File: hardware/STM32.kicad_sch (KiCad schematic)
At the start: 15 parts, among them U1 STM32U595RJTxQ

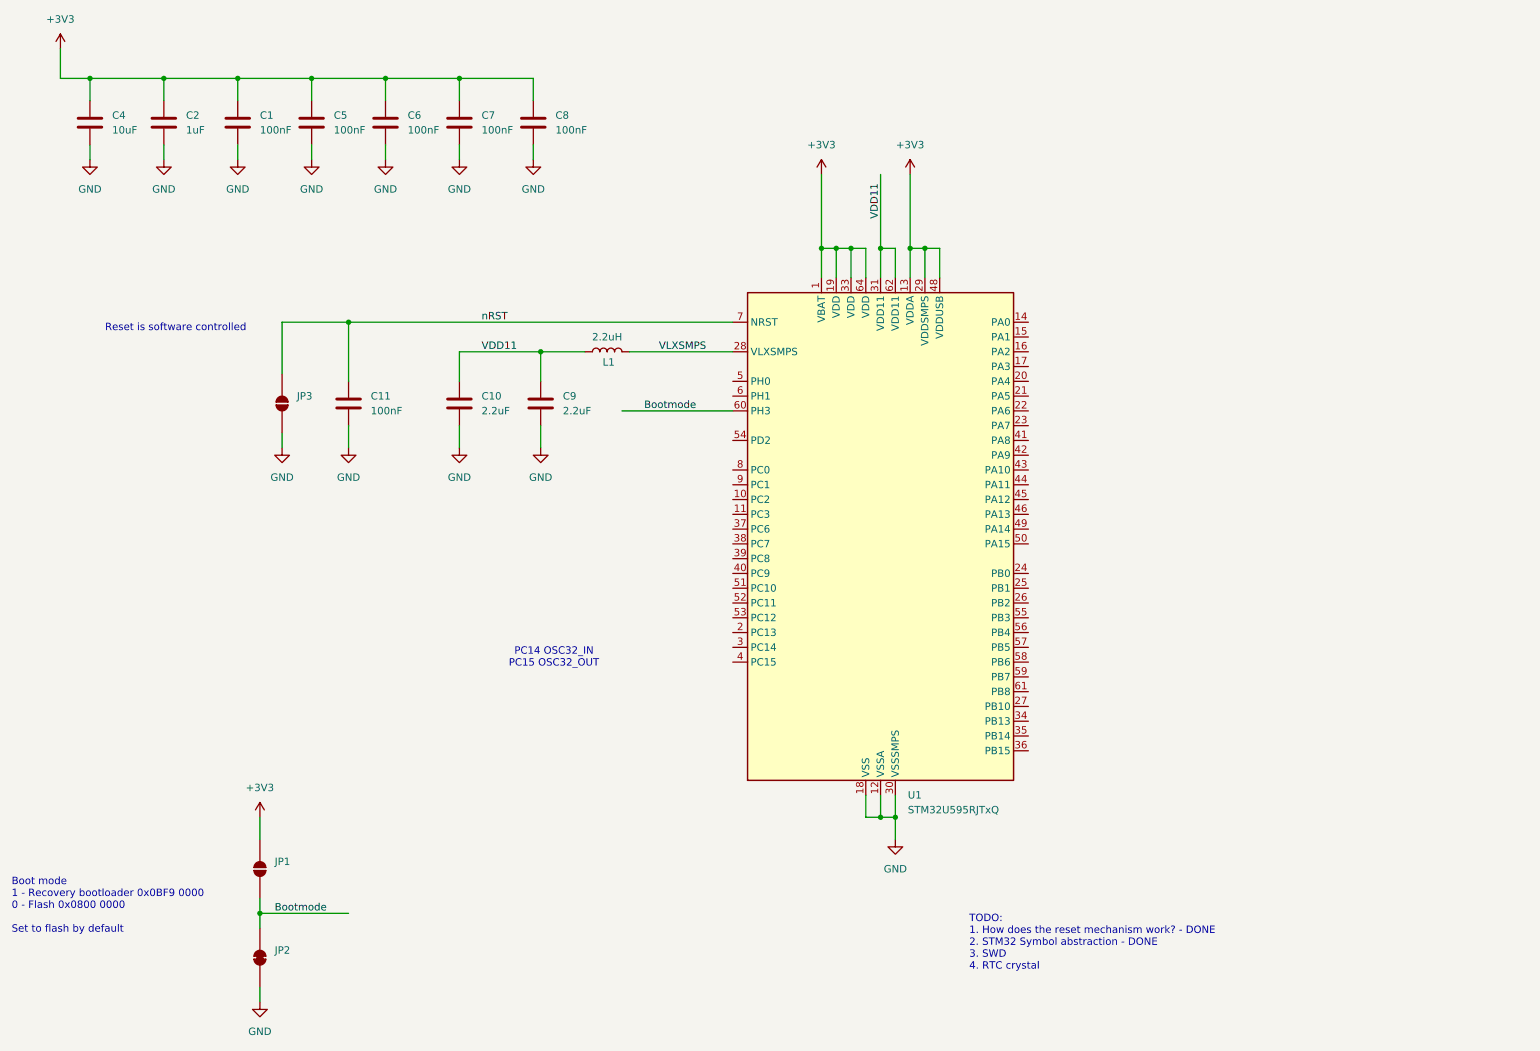
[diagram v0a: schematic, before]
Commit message: Completed STM32 schematic
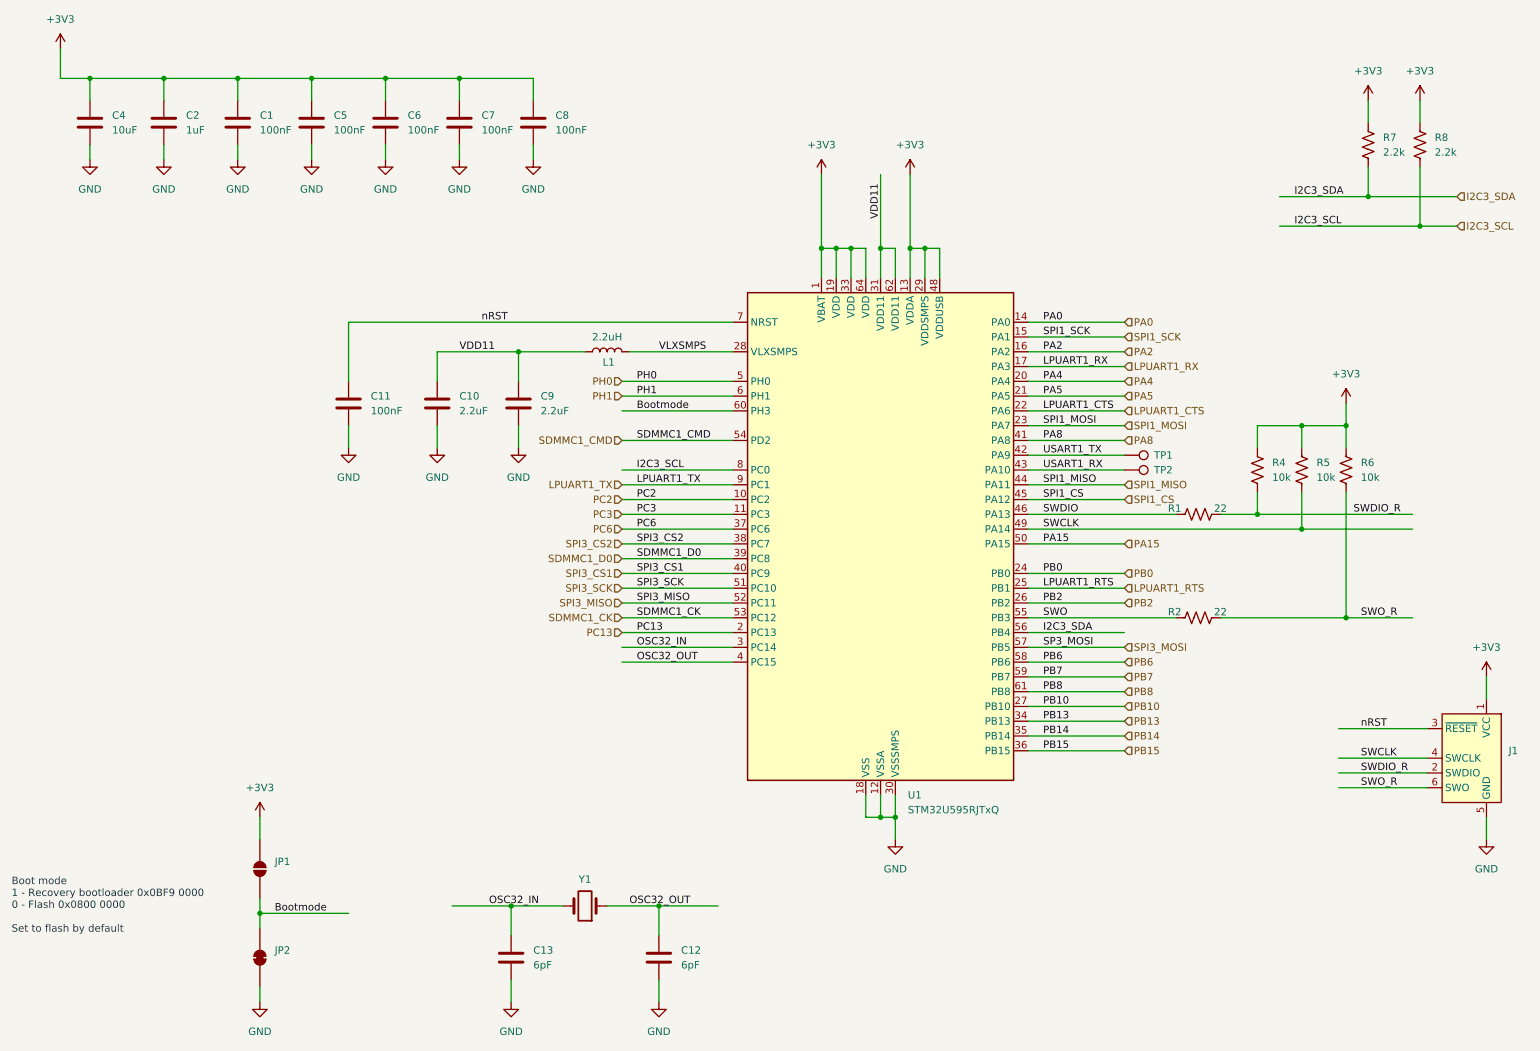
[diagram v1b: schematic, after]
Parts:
- removed JP3: SolderJumper_2_Open, symbol Jumper:SolderJumper_2_Open
- added C12, C13: 6pF, symbol Device:C
- added J1: Conn_ARM_SWD_TagConnect_TC2030-NL, Connector:Tag-Connect_TC2030-IDC-NL_2x03_P1.27mm_Vertical, symbol Connector:Conn_ARM_SWD_TagConnect_TC2030-NL
- added R1, R2: 22, symbol Device:R_US
- added R4, R5, R6: 10k, symbol Device:R_US
- added R7, R8: 2.2k, symbol Device:R_US
- added TP1, TP2: TestPoint, symbol Connector:TestPoint
- added Y1: ECS-.327-6-12R-TR, symbol Device:Crystal
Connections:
- net +3V3: now also J1.1 (VCC), R4.2, R5.2, R6.2, R7.2, R8.2
- net GND: now also C12.2, C13.2, J1.5 (GND)
- net nRST: now also J1.3 (~{RESET})
- net PC2: now reaches U1.10 (PC2)
- net PC3: now reaches U1.11 (PC3)
- net PA0: now reaches U1.14 (PA0)
- net SPI1_SCK: now reaches U1.15 (PA1)
- net PA2: now reaches U1.16 (PA2)
- net LPUART1_RX: now reaches U1.17 (PA3)
- net PC13: now reaches U1.2 (PC13)
- net PA4: now reaches U1.20 (PA4)
- net PA5: now reaches U1.21 (PA5)
- net LPUART1_CTS: now reaches U1.22 (PA6)
- net SPI1_MOSI: now reaches U1.23 (PA7)
- net PB0: now reaches U1.24 (PB0)
- net LPUART1_RTS: now reaches U1.25 (PB1)
- net PB2: now reaches U1.26 (PB2)
- net PB10: now reaches U1.27 (PB10)
- net OSC32_IN: now reaches U1.3 (PC14)
- net OSC32_IN: now also C13.1, Y1.2
- net PB13: now reaches U1.34 (PB13)
- net PB14: now reaches U1.35 (PB14)
- net PB15: now reaches U1.36 (PB15)
- net PC6: now reaches U1.37 (PC6)
- net SPI3_CS2: now reaches U1.38 (PC7)
- net SDMMC1_D0: now reaches U1.39 (PC8)
- net OSC32_OUT: now reaches U1.4 (PC15)
- net OSC32_OUT: now also C12.1, Y1.1
- net SPI3_CS1: now reaches U1.40 (PC9)
- net PA8: now reaches U1.41 (PA8)
- net USART1_TX: now reaches U1.42 (PA9)
- net USART1_TX: now also TP1.1
- net USART1_RX: now reaches U1.43 (PA10)
- net USART1_RX: now also TP2.1
- net SPI1_MISO: now reaches U1.44 (PA11)
- net SPI1_CS: now reaches U1.45 (PA12)
- net SWDIO: now reaches U1.46 (PA13)
- net SWDIO: now also R1.1
- net SWCLK: now reaches U1.49 (PA14)
- net SWCLK: now also J1.4 (SWCLK), R5.1
- net PH0: now reaches U1.5 (PH0)
- net PA15: now reaches U1.50 (PA15)
- net SPI3_SCK: now reaches U1.51 (PC10)
- net SPI3_MISO: now reaches U1.52 (PC11)
- net SDMMC1_CK: now reaches U1.53 (PC12)
- net SDMMC1_CMD: now reaches U1.54 (PD2)
- net SWO: now reaches U1.55 (PB3)
- net SWO: now also R2.1
- net I2C3_SDA: now reaches U1.56 (PB4)
- net I2C3_SDA: now also R7.1
- net SPI3_MOSI: now reaches U1.57 (PB5)
- net PB6: now reaches U1.58 (PB6)
- net PB7: now reaches U1.59 (PB7)
- net PH1: now reaches U1.6 (PH1)
- net PB8: now reaches U1.61 (PB8)
- net I2C3_SCL: now reaches U1.8 (PC0)
- net I2C3_SCL: now also R8.1
- net LPUART1_TX: now reaches U1.9 (PC1)
- new net SWDIO_R: J1.2 (SWDIO), R1.2, R4.1
- new net SWO_R: J1.6 (SWO), R2.2, R6.1
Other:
- note removed: "PC14 OSC32_IN PC15 OSC32_OUT"
- note removed: "Reset is software controlled"
- note removed: "TODO: 1. How does the reset mechanism work? - DONE 2. STM32 Symbol abstraction - DONE 3. SWD 4. RTC crystal"
- moved on the sheet: C10, C9

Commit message: Completed STM32 high level block and connected eMMC
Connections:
- net SPI1_CS renamed SPI1_CS1
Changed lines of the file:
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@@
+	(wire
+		(pts
+			(xy 73.66 67.31) (xy 139.7 67.31)
+		)
+		(stroke
+			(width 0)
+			(type default)
+		)
+	)
 	(wire
 		(pts
@@
 		(pts
 			(xy 245.11 96.52) (xy 245.11 118.11)
-		)
-		(stroke
-			(width 0)
-			(type default)
-		)
-	)
-	(wire
-		(pts
-			(xy 139.7 67.31) (xy 73.66 67.31)
 		)
 		(stroke
@@
 	)
 	(label "nRST"
-		(at 96.52 67.31 0)
+		(at 92.71 67.31 0)
 		(effects
 			(font
@@
 		)
 	)
-	(label "SPI1_CS"
+	(label "SPI1_CS1"
 		(at 193.04 97.79 0)
 		(effects
@@
 		)
 	)
-	(hierarchical_label "SPI1_CS"
+	(hierarchical_label "SPI1_CS1"
 		(shape input)
 		(at 207.01 97.79 0)

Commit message: Added PPG schematic page
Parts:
- added TP11, TP12, TP13, TP14: TestPoint, symbol Connector:TestPoint
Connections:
- net +3V3: now also TP14.1
- net VDD11: now also TP12.1
- net VLXSMPS: now also TP11.1
- net nRST: now also TP13.1

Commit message: Added display block (barely) and freaked out about PPG stuff
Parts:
- added TP15: TestPoint, symbol Connector:TestPoint
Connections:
- net Bootmode: now also TP15.1
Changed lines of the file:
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@@
+	)
+	(symbol
+		(lib_id "Connector:TestPoint")
+		(at 73.66 168.91 270)
+		(unit 1)
+		(body_style 1)
+		(exclude_from_sim no)
+		(in_bom yes)
+		(on_board yes)
+		(in_pos_files yes)
+		(dnp no)
+		(property "Reference" "TP15"
+			(at 78.74 168.91 90)
+			(show_name no)
+			(do_not_autoplace no)
+			(effects
+				(font
+					(size 1.27 1.27)
+				)
+				(justify left)
+			)
+		)
+		(property "Value" "TestPoint"
+			(at 78.74 170.1799 90)
+			(hide yes)
+			(show_name no)
+			(do_not_autoplace no)
+			(effects
+				(font
+					(size 1.27 1.27)
+				)
+				(justify left)
+			)
+		)
+		(property "Footprint" ""
+			(at 73.66 173.99 0)
+			(hide yes)
+			(show_name no)
+			(do_not_autoplace no)
+			(effects
+				(font
+					(size 1.27 1.27)
+				)
+			)
+		)
+		(property "Datasheet" ""
+			(at 73.66 173.99 0)
+			(hide yes)
+			(show_name no)
+			(do_not_autoplace no)
+			(effects
+				(font
+					(size 1.27 1.27)
+				)
+			)
+		)
+		(property "Description" "test point"
+			(at 73.66 168.91 0)
+			(hide yes)
+			(show_name no)
+			(do_not_autoplace no)
+			(effects
+				(font
+					(size 1.27 1.27)
+				)
+			)
+		)
+		(pin "1"
+		)
+		(instances
+			(project "hardware"
+				(path "/a19f636f-b28d-4c43-b96a-b02383edd3eb/66e2f96f-c2f9-49fe-949d-95863aff4e55/1bcdaece-dced-4ca9-bf09-f705a839e6b8"
+					(reference "TP15")
+					(unit 1)
+				)
+			)
+		)
 	)
 	(symbol

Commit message: Added bluetooth module schematic and environmental perception block"
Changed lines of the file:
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@@
 		)
 		(property "Value" "ECS-.327-6-12R-TR"
-			(at 114.3 162.56 0)
-			(hide yes)
+			(at 114.3 171.958 0)
 			(show_name no)
 			(do_not_autoplace no)

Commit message: Changing barometer, STM32 and power rails
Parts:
- removed U1: STM32U595RJTxQ, Package_QFP:LQFP-64_10x10mm_P0.5mm, symbol MCU_ST_STM32U5:STM32U595RJTxQ
- added U1: STM32U5A5QJIxQ, Package_BGA:UFBGA-132_7x7mm_Layout12x12_P0.5mm, symbol MCU_ST_STM32U5:STM32U5A5QJIxQ
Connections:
- new net: U1.E4 (VSS), U1.E9 (VSS), U1.F6 (VSS), U1.G7 (VSS), U1.H4 (VSS), U1.H9 (VSS)
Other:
- moved on the sheet: C10, C11, C12, C13, C9, J1, JP1, JP2, L1, R1, R2, R4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

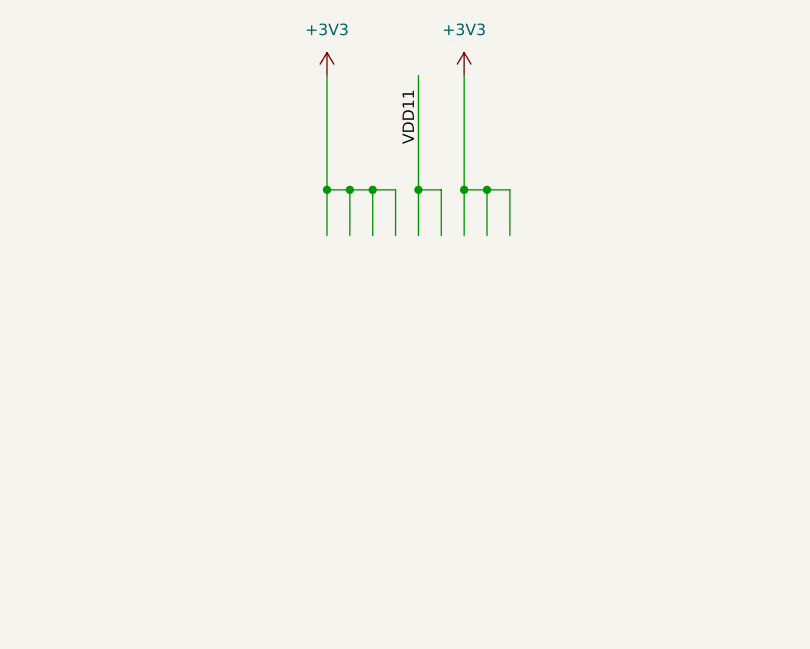
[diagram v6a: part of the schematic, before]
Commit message: Added optical front end submodule and reconnected to STM32
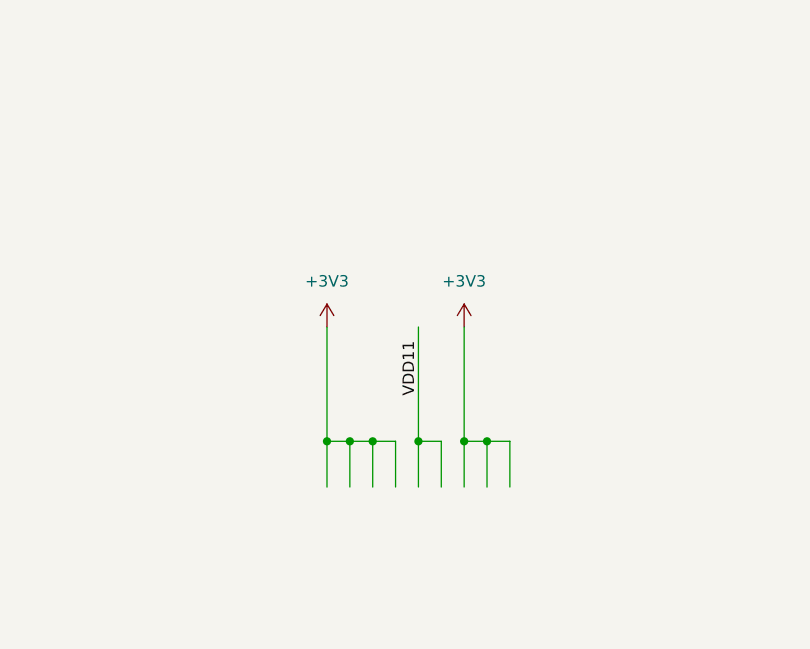
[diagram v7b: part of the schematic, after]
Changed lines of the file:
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@@
 	)
 	(junction
-		(at 292.1 10.16)
+		(at 292.1 38.1)
 		(diameter 0)
 		(color 0 0 0 0)
@@
 	)
 	(junction
-		(at 307.34 10.16)
+		(at 307.34 38.1)
 		(diameter 0)
 		(color 0 0 0 0)
@@
 	)
 	(junction
-		(at 304.8 10.16)
+		(at 304.8 38.1)
 		(diameter 0)
 		(color 0 0 0 0)
@@
 	)
 	(junction
-		(at 299.72 10.16)
+		(at 299.72 38.1)
 		(diameter 0)
 		(color 0 0 0 0)
@@
 	)
 	(junction
-		(at 294.64 10.16)
+		(at 294.64 38.1)
 		(diameter 0)
 		(color 0 0 0 0)
@@
 	)
 	(junction
-		(at 289.56 10.16)
+		(at 289.56 38.1)
 		(diameter 0)
 		(color 0 0 0 0)
@@
 	(wire
 		(pts
-			(xy 292.1 10.16) (xy 289.56 10.16)
+			(xy 292.1 38.1) (xy 289.56 38.1)
 		)
 		(stroke
@@
 	(wire
 		(pts
-			(xy 292.1 15.24) (xy 292.1 10.16)
+			(xy 292.1 43.18) (xy 292.1 38.1)
 		)
 		(stroke
@@
 	(wire
 		(pts
-			(xy 289.56 10.16) (xy 289.56 15.24)
+			(xy 289.56 38.1) (xy 289.56 43.18)
 		)
 		(stroke
@@
 	(wire
 		(pts
-			(xy 302.26 10.16) (xy 299.72 10.16)
+			(xy 302.26 38.1) (xy 299.72 38.1)
 		)
 		(stroke
@@
 	(wire
 		(pts
-			(xy 302.26 15.24) (xy 302.26 10.16)
+			(xy 302.26 43.18) (xy 302.26 38.1)
 		)
 		(stroke
@@
 	(wire
 		(pts
-			(xy 299.72 -2.54) (xy 299.72 10.16)
+			(xy 299.72 25.4) (xy 299.72 38.1)
 		)
 		(stroke
@@
 	(wire
 		(pts
-			(xy 294.64 15.24) (xy 294.64 10.16)
+			(xy 294.64 43.18) (xy 294.64 38.1)
 		)
 		(stroke
@@
 	(wire
 		(pts
-			(xy 289.56 -2.54) (xy 289.56 10.16)
+			(xy 289.56 25.4) (xy 289.56 38.1)
 		)
 		(stroke
@@
 	(wire
 		(pts
-			(xy 309.88 15.24) (xy 309.88 10.16)
+			(xy 309.88 43.18) (xy 309.88 38.1)
 		)
 		(stroke
@@
 	(wire
 		(pts
-			(xy 294.64 10.16) (xy 292.1 10.16)
+			(xy 294.64 38.1) (xy 292.1 38.1)
 		)
 		(stroke
@@
 	(wire
 		(pts
-			(xy 309.88 10.16) (xy 307.34 10.16)
+			(xy 309.88 38.1) (xy 307.34 38.1)
 		)
 		(stroke
@@
 	(wire
 		(pts
-			(xy 304.8 10.16) (xy 307.34 10.16)
+			(xy 304.8 38.1) (xy 307.34 38.1)
 		)
 		(stroke
@@
 	(wire
 		(pts
-			(xy 297.18 10.16) (xy 294.64 10.16)
+			(xy 297.18 38.1) (xy 294.64 38.1)
 		)
 		(stroke
@@
 	(wire
 		(pts
-			(xy 299.72 10.16) (xy 299.72 15.24)
+			(xy 299.72 38.1) (xy 299.72 43.18)
 		)
 		(stroke
@@
 	(wire
 		(pts
-			(xy 297.18 15.24) (xy 297.18 10.16)
+			(xy 297.18 43.18) (xy 297.18 38.1)
 		)
 		(stroke
@@
 	(wire
 		(pts
-			(xy 304.8 15.24) (xy 304.8 10.16)
+			(xy 304.8 43.18) (xy 304.8 38.1)
 		)
 		(stroke
@@
 	(wire
 		(pts
-			(xy 304.8 -2.54) (xy 304.8 10.16)
+			(xy 304.8 25.4) (xy 304.8 38.1)
 		)
 		(stroke
@@
 	(wire
 		(pts
-			(xy 307.34 15.24) (xy 307.34 10.16)
+			(xy 307.34 43.18) (xy 307.34 38.1)
 		)
 		(stroke
@@
 	)
 	(label "VDD11"
-		(at 299.72 5.08 90)
+		(at 299.72 33.02 90)
 		(effects
 			(font
@@
 	(symbol
 		(lib_id "power:+3V3")
-		(at 289.56 -2.54 0)
+		(at 289.56 25.4 0)
 		(unit 1)
 		(body_style 1)
@@
 		(fields_autoplaced yes)
 		(property "Reference" "#PWR06"
-			(at 289.56 1.27 0)
+			(at 289.56 29.21 0)
 			(hide yes)
 			(show_name no)
@@
 		)
 		(property "Value" "+3V3"
-			(at 289.56 -7.62 0)
+			(at 289.56 20.32 0)
 			(show_name no)
 			(do_not_autoplace no)
@@
 		)
 		(property "Footprint" ""
-			(at 289.56 -2.54 0)
+			(at 289.56 25.4 0)
 			(hide yes)
 			(show_name no)
@@
 		)
 		(property "Datasheet" ""
-			(at 289.56 -2.54 0)
+			(at 289.56 25.4 0)
 			(hide yes)
 			(show_name no)
@@
 		)
 		(property "Description" "Power symbol creates a global label with name \"+3V3\""
-			(at 289.56 -2.54 0)
+			(at 289.56 25.4 0)
 			(hide yes)
 			(show_name no)
@@
 	(symbol
 		(lib_id "power:+3V3")
-		(at 304.8 -2.54 0)
+		(at 304.8 25.4 0)
 		(unit 1)
 		(body_style 1)
@@
 		(fields_autoplaced yes)
 		(property "Reference" "#PWR08"
-			(at 304.8 1.27 0)
+			(at 304.8 29.21 0)
 			(hide yes)
 			(show_name no)
@@
 		)
 		(property "Value" "+3V3"
-			(at 304.8 -7.62 0)
+			(at 304.8 20.32 0)
 			(show_name no)
 			(do_not_autoplace no)
@@
 		)
 		(property "Footprint" ""
-			(at 304.8 -2.54 0)
+			(at 304.8 25.4 0)
 			(hide yes)
 			(show_name no)
@@
 		)
 		(property "Datasheet" ""
-			(at 304.8 -2.54 0)
+			(at 304.8 25.4 0)
 			(hide yes)
 			(show_name no)
@@
 		)
 		(property "Description" "Power symbol creates a global label with name \"+3V3\""
-			(at 304.8 -2.54 0)
+			(at 304.8 25.4 0)
 			(hide yes)
 			(show_name no)

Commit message: Contemplating switching back to the 64LQFP
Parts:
- added C47, C50, C53, C54: 0.1uF, symbol Device:C
- added C48: 10uF, symbol Device:C
- added C49: 4.7uF, symbol Device:C
- added C51, C52: 1uF, symbol Device:C
- added TP24: TestPoint, symbol Connector:TestPoint
- C1, C5, C6, C7: value 100nF -> 0.1uF
- C2: value 1uF -> 0.1uF
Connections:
- net Bootmode is gone; now on net BOOTMODE: JP1.1 (A), JP2.2 (B), TP15.1
- net +3V3: now also U1.D8 (VDDIO2), C49.2, C53.2, TP24.1; no longer C1.1, C2.1, C4.1, C5.1, C6.1, C7.1, C8.1, R7.2, R8.2, TP14.1
- net GND: now also C8.1, U1.E4 (VSS), U1.E9 (VSS), U1.F6 (VSS), U1.G7 (VSS), U1.H1 (VSSA), U1.H4 (VSS), U1.H9 (VSS), U1.L10 (VSSSMPS), C47.2, C48.1, C49.1, C50.1, C51.1, C52.1, C53.1, C54.2; no longer C8.2
- net LPUART1_CTS: now also U1.K10 (PB13)
- net LPUART1_RTS: now also U1.L11 (PB12)
- net LPUART1_RX: now also U1.K9 (PB10)
- net LPUART1_TX: now also U1.L9 (PB11)
- net OSC32_IN: now also U1.C1 (PC14)
- net OSC32_OUT: now also U1.D1 (PC15)
- net SPI3_MISO: now also U1.B6 (PB4)
- net SPI3_MOSI: now also U1.A7 (PD6)
- net SPI3_SCK: now also U1.B11 (PC10)
- net SWCLK: now also R6.1, U1.C11 (PA14); no longer R5.1
- net SWDIO: now also U1.C10 (PA13)
- net SWDIO_R: now also R5.1; no longer R4.1
- net SWO: now also U1.C6 (PB3)
- net SWO_R: now also R4.1; no longer R6.1
- net VDD11: now also U1.B4 (VDD11), U1.M11 (VDD11)
- net VLXSMPS: now also U1.M10 (VLXSMPS)
- net nRST: now also U1.G2 (NRST)
- net +1V8: now reaches U1.A12 (VDDUSB)
- net +1V8: now also C1.1, C2.1, C4.1, C5.1, C6.1, C7.1, C8.2, R7.2, R8.2, TP14.1, U1.B1 (VBAT), U1.D4 (VDD), U1.D9 (VDD), U1.F7 (VDD), U1.G6 (VDD), U1.J1 (VREF+), U1.J4 (VDD), U1.J9 (VDD), U1.K1 (VDDA), U1.M9 (VDDSMPS), C47.1, C48.2, C50.2, C51.2, C52.2, C54.1
- net BOOTMODE: now reaches U1.B5 (PH3)
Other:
- note added: "TODO: Drive SPI3 CS pins with LPGPIO1"
- moved on the sheet: C1, C10, C11, C12, C13, C2, C5, C6, C7, C9, J1, L1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
